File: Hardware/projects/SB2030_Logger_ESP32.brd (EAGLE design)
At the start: 32.7 x 59.7 mm, 20 parts, among them SW1 CKTACTSWITCH, U1 ESP-WROOM-32, U2 MCP2562, U3 NCP1117ST50T3G, U4 NCP1117ST33T3G

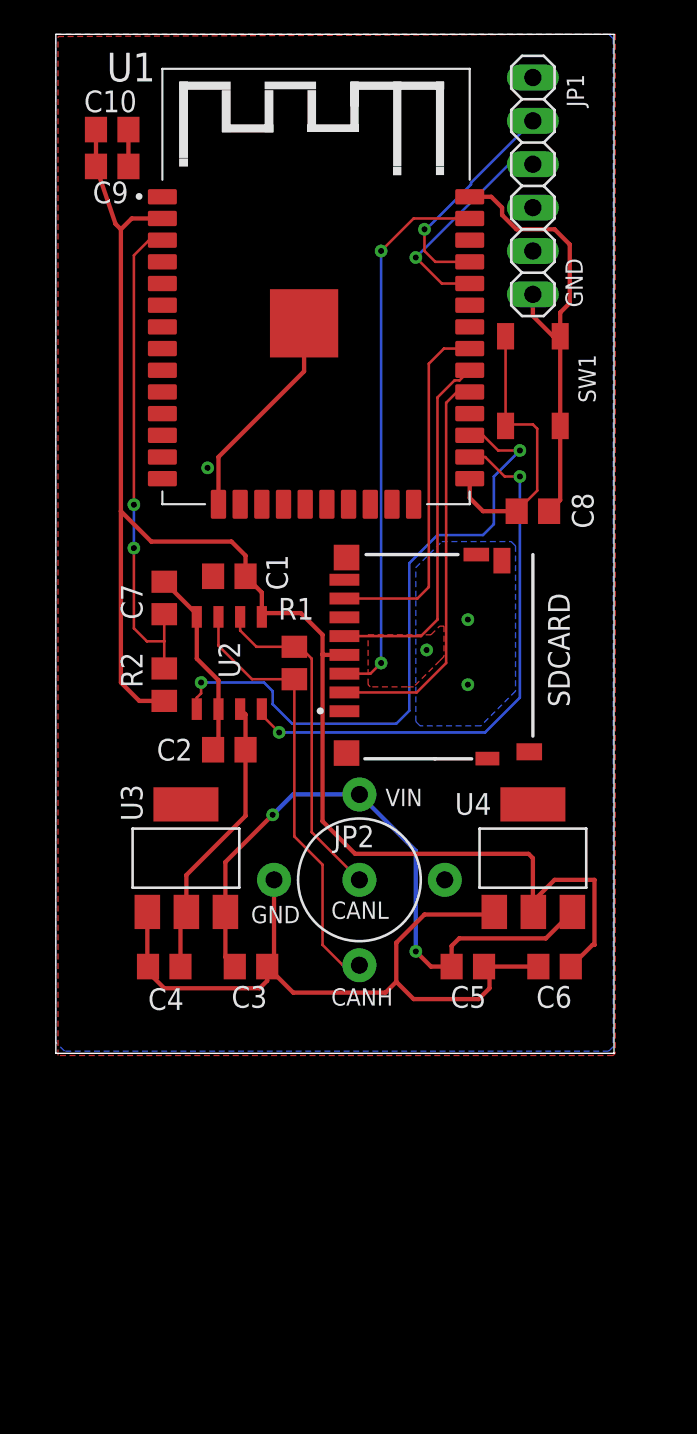
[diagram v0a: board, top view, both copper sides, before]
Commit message: Updates to hardware prototype design to support RS422 input, and added separate RS422 for Arduino Due for testing purposes.
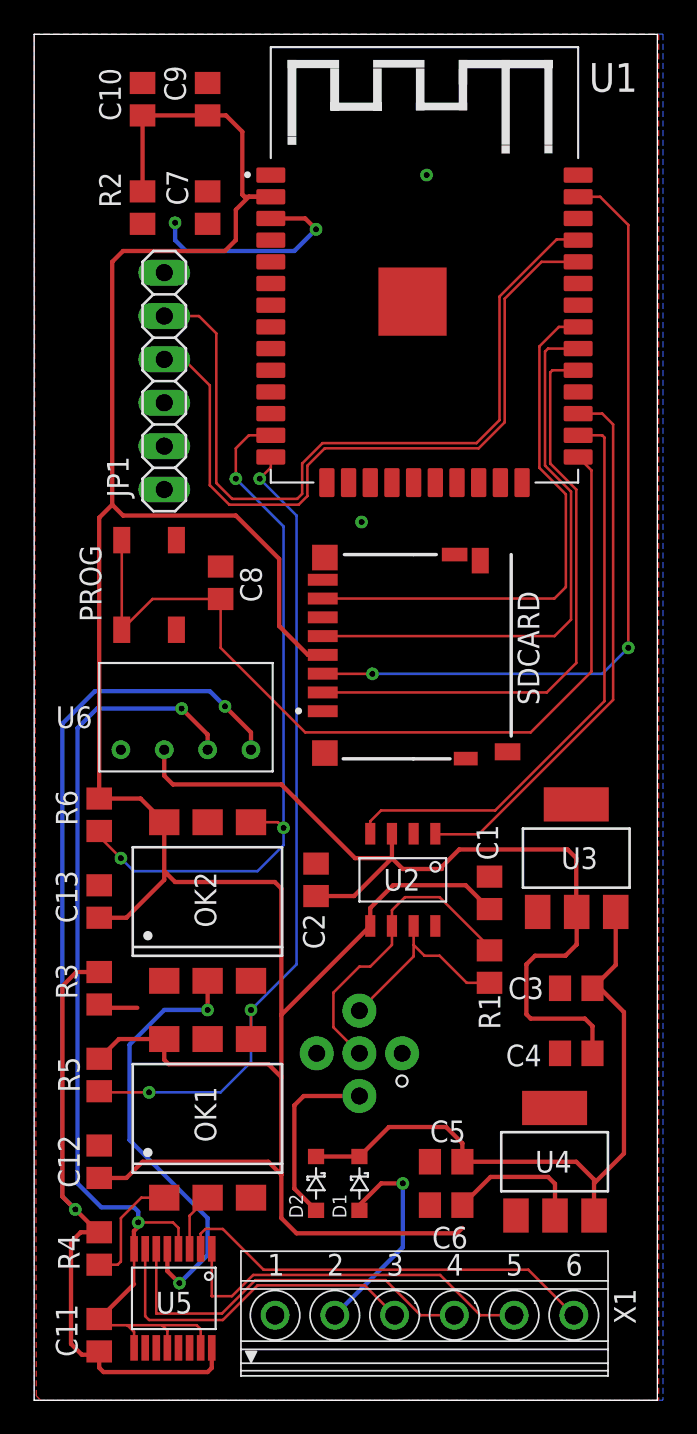
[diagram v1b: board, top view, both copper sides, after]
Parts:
- added C11, C12, C13: 0.1u, rcl:C0805
- added D1, D2: 1N5819, sb2030_logger:SOD123
- added OK1, OK2: H11L1MS, optocoupler:DIL6-SMD
- added R3, R4: 1k2, rcl:R0805
- added R5, R6: 10k, rcl:R0805
- added U5: SN65C1168PWR, sb2030_logger:16-TSSOP
- added U6: (no value), sb2030_logger:RFM-0505S
- added X1: 1751280, con-phoenix-350:1751280
- moved R2 28.0 mm to (6.35, 69.8), turned to 90 degrees
- moved SW1 25.5 mm to (6.73, 47.8)
- moved C4 24.7 mm to (31.8, 20.3)
- moved JP1 24.4 mm to (7.62, 59.7)
- moved C1 24.0 mm to (26.7, 29.7), turned to 90 degrees
- moved C7 23.0 mm to (10.2, 69.8)
- moved U3 22.9 mm to (31.8, 31.8)
- moved R1 21.1 mm to (26.7, 25.4)
- moved C3 19.1 mm to (31.8, 24.1), turned to 180 degrees
- moved C8 18.8 mm to (10.9, 47.9), turned to 90 degrees
- moved U4 17.8 mm to (30.5, 14.0)
- moved U2 16.3 mm to (21.6, 30.5), turned to 180 degrees
- moved C6 15.3 mm to (24.1, 11.4)
- moved C5 11.5 mm to (24.1, 14.0), turned to 180 degrees
- moved JP2 10.2 mm to (19.1, 20.3)
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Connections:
- removed net N$11: C1.2
- new net +12V: D1.1, X1.2
- new net GNDI: C11.2, U5.12, U5.15, U5.4, U5.8, U5.9, U6.3
- new net N$13: OK1.2, U5.3
- new net N$14: OK2.2, U5.5
- new net N$15: OK1.1, R4.1
- new net N$16: OK2.1, R3.1
- new net N$17: U5.2, X1.6
- new net N$18: U5.1, X1.5
- new net N$19: U5.6, X1.4
- new net N$20: U5.7, X1.3
- new net N$21: C11.1, R3.2, R4.2, U5.16, U6.4
- new net N$22: D2.1, JP2.2
- new net RX1: OK1.4, R5.1, U1.14
- new net RX2: OK2.4, R6.1, U1.13
- net +3V3: now also C12.1, C13.1, OK1.6, OK2.6, R5.2, R6.2
- net +5V: now also U6.2
- net GND: now also C1.2, C12.2, C13.2, OK1.5, OK2.5, U6.1, X1.1
- net VIN: now also D1.2, D2.2; no longer JP2.2
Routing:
- net GND: track 98.0 -> 0.00 mm, vias 4 -> 2
- net +3V3: track 93.4 -> 177.0 mm
- net N$21: track 0.00 -> 79.2 mm, vias 0 -> 2
- net GNDI: track 0.00 -> 62.1 mm, vias 0 -> 2
- net RX1: track 0.00 -> 49.1 mm, vias 0 -> 3
- net RX2: track 0.00 -> 41.4 mm, vias 0 -> 3
- net N$12: track 16.8 -> 52.8 mm
- net +5V: track 16.8 -> 52.6 mm
- net RXDATA: track 13.2 -> 45.4 mm, vias 1 -> 0
- net TXDATA: track 12.9 -> 42.4 mm, vias 1 -> 0
- net N$14: track 0.00 -> 26.0 mm, vias 0 -> 2
- net N$17: track 0.00 -> 25.0 mm
- net N$19: track 0.00 -> 22.9 mm
- net N$18: track 0.00 -> 22.0 mm
- net N$20: track 0.00 -> 20.2 mm
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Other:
- board size 32.7 x 59.7 mm -> 36.5 x 80 mm
- board text added: "PROG"
- board text removed: "CANH"
- board text removed: "CANL"
- board text removed: "GND"
- board text removed: "JP2"
- board text removed: "SW1"
- board text removed: "VIN"

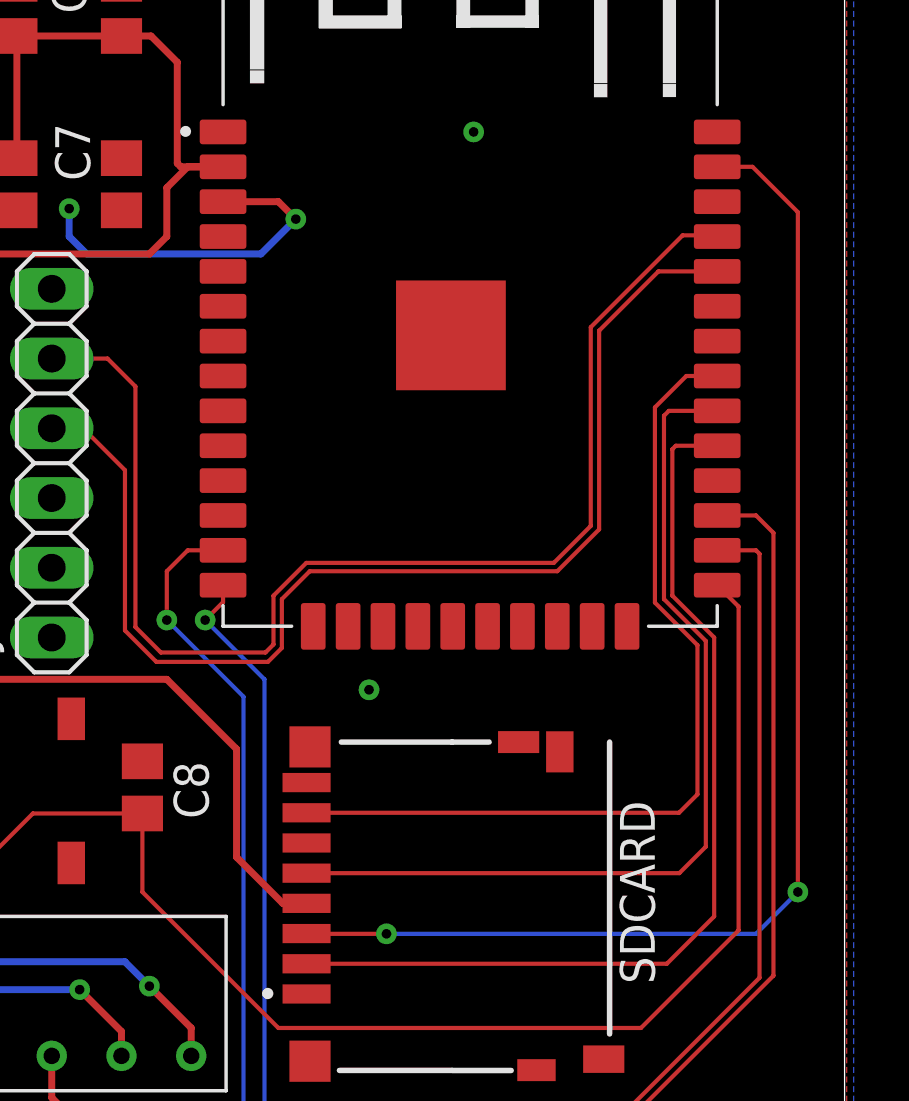
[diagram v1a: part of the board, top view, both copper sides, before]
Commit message: Update to ESP32-based hardware to accommodate NMEA0183 input pins that don't cause boot problems (GPIO12 is used to set Flash voltage on boot, so having an active data stream attached causes all sorts of problems at boot time).
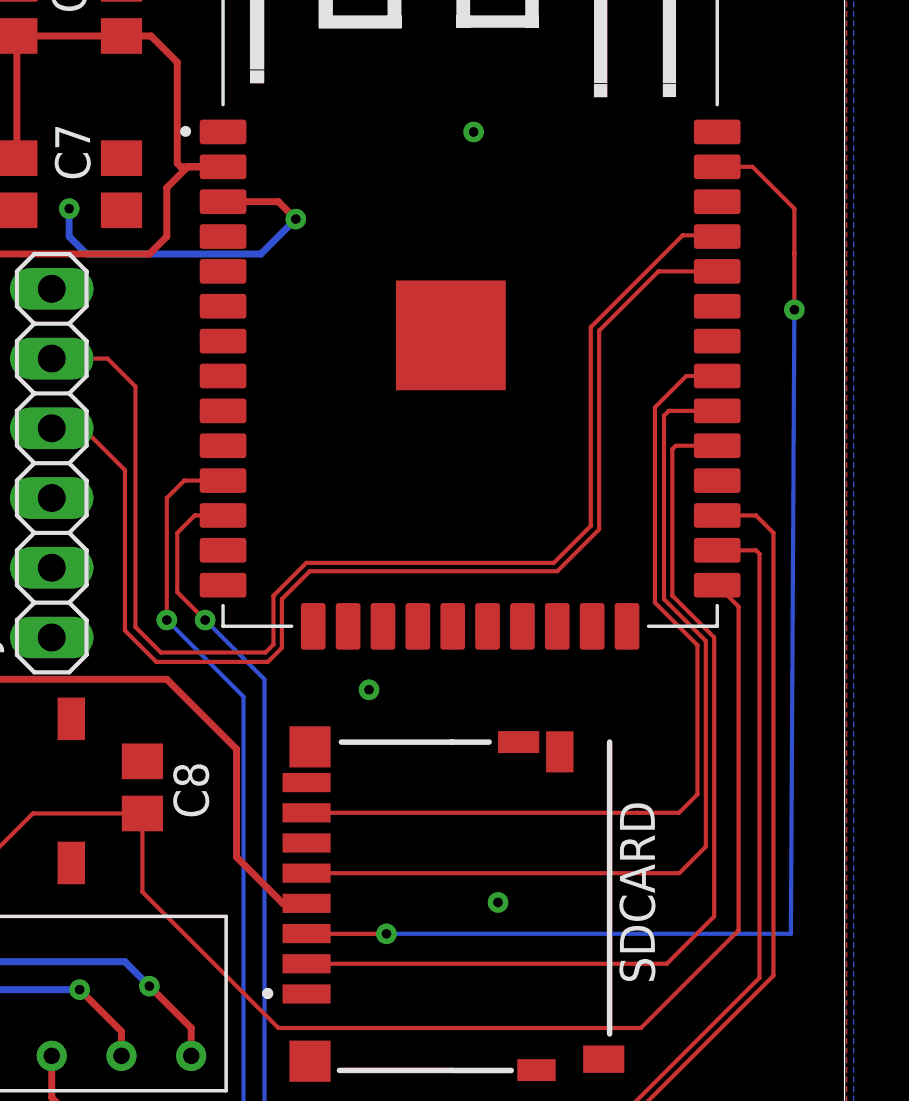
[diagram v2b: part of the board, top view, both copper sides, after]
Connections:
- net RX1: now also U1.12; no longer U1.14
- net RX2: now also U1.11; no longer U1.13
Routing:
- net RX1: track 49.1 -> 53.0 mm
- net RX2: track 41.4 -> 44.0 mm
- net N$8: track 46.9 -> 47.5 mm
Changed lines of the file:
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@@
 <drawing>
 <settings>
-<setting alwaysvectorfont="yes"/>
+<setting alwaysvectorfont="no"/>
 <setting verticaltext="up"/>
 </settings>
@@
 <via x="19.177" y="51.435" extent="1-16" drill="0.35"/>
 <via x="22.987" y="71.755" extent="1-16" drill="0.35"/>
+<via x="23.876" y="43.688" extent="1-16" drill="0.35"/>
 </signal>
 <signal name="+3V3">
@@
 <contactref element="U1" pad="37"/>
 <contactref element="SDCARD" pad="3"/>
-<wire x1="31.86" y1="70.485" x2="33.147" y2="70.485" width="0.1524" layer="1"/>
-<wire x1="33.147" y1="70.485" x2="34.798" y2="68.834" width="0.1524" layer="1"/>
-<wire x1="34.798" y1="68.834" x2="34.798" y2="44.069" width="0.1524" layer="1"/>
-<via x="34.798" y="44.069" extent="1-16" drill="0.35"/>
-<wire x1="34.798" y1="44.069" x2="33.274" y2="42.545" width="0.1524" layer="16"/>
-<wire x1="33.274" y1="42.545" x2="19.812" y2="42.545" width="0.1524" layer="16"/>
+<wire x1="33.147" y1="70.485" x2="31.86" y2="70.485" width="0.1524" layer="1"/>
+<wire x1="34.671" y1="67.35618125" x2="34.671" y2="67.31" width="0.1524" layer="1"/>
+<via x="34.671" y="65.278" extent="1-16" drill="0.35"/>
+<wire x1="34.671" y1="67.31" x2="34.671" y2="65.278" width="0.1524" layer="1"/>
+<wire x1="34.671" y1="65.278" x2="34.544" y2="42.545" width="0.1524" layer="16"/>
+<wire x1="34.544" y1="42.545" x2="19.812" y2="42.545" width="0.1524" layer="16"/>
 <via x="19.812" y="42.545" extent="1-16" drill="0.35"/>
 <wire x1="19.812" y1="42.545" x2="16.912" y2="42.545" width="0.1524" layer="1"/>
 <wire x1="16.912" y1="42.545" x2="16.902" y2="42.555" width="0.1524" layer="1"/>
+<wire x1="34.671" y1="67.35618125" x2="34.671" y2="68.961" width="0.1524" layer="1"/>
+<wire x1="34.671" y1="68.961" x2="33.147" y2="70.485" width="0.1524" layer="1"/>
 </signal>
 <signal name="N$9">
@@
 </signal>
 <signal name="RX1">
-<contactref element="U1" pad="14"/>
 <contactref element="OK1" pad="4"/>
 <contactref element="R5" pad="1"/>
@@
 <wire x1="15.367" y1="51.816" x2="13.208" y2="53.975" width="0.1524" layer="16"/>
 <via x="13.208" y="53.975" extent="1-16" drill="0.35"/>
-<wire x1="13.208" y1="53.975" x2="13.86" y2="54.627" width="0.1524" layer="1"/>
-<wire x1="13.86" y1="54.627" x2="13.86" y2="55.245" width="0.1524" layer="1"/>
+<contactref element="U1" pad="12"/>
+<wire x1="13.208" y1="53.975" x2="12.192" y2="54.991" width="0.1524" layer="1"/>
+<wire x1="12.192" y1="54.991" x2="12.192" y2="57.15" width="0.1524" layer="1"/>
+<wire x1="12.192" y1="57.15" x2="12.827" y2="57.785" width="0.1524" layer="1"/>
+<wire x1="12.827" y1="57.785" x2="13.86" y2="57.785" width="0.1524" layer="1"/>
 </signal>
 <signal name="RX2">
-<contactref element="U1" pad="13"/>
 <contactref element="OK2" pad="4"/>
 <contactref element="R6" pad="1"/>
@@
 <wire x1="14.605" y1="51.181" x2="11.811" y2="53.975" width="0.1524" layer="16"/>
 <via x="11.811" y="53.975" extent="1-16" drill="0.35"/>
-<wire x1="11.811" y1="53.975" x2="11.811" y2="55.753" width="0.1524" layer="1"/>
-<wire x1="11.811" y1="55.753" x2="12.573" y2="56.515" width="0.1524" layer="1"/>
-<wire x1="12.573" y1="56.515" x2="13.86" y2="56.515" width="0.1524" layer="1"/>
+<contactref element="U1" pad="11"/>
+<wire x1="12.446" y1="59.055" x2="13.86" y2="59.055" width="0.1524" layer="1"/>
+<wire x1="11.811" y1="53.975" x2="11.811" y2="58.42" width="0.1524" layer="1"/>
+<wire x1="11.811" y1="58.42" x2="12.446" y2="59.055" width="0.1524" layer="1"/>
 </signal>
 <signal name="N$22">

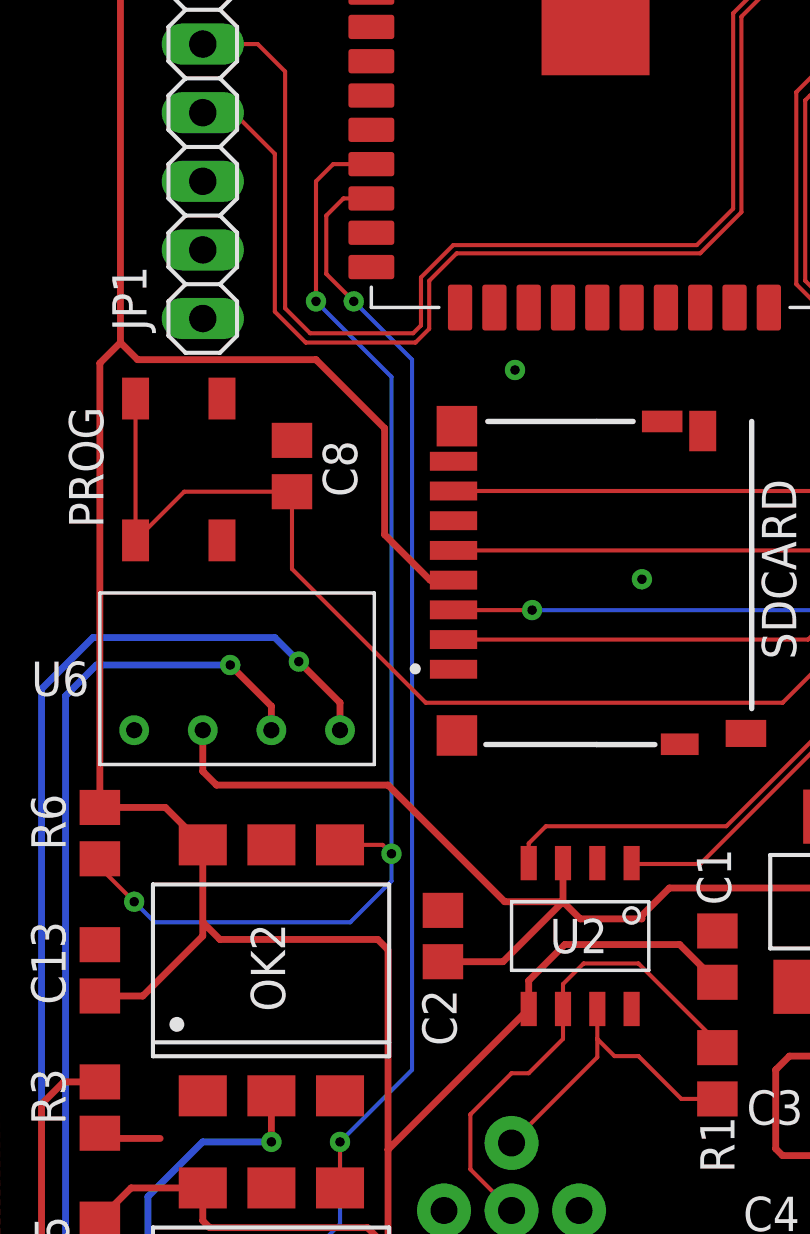
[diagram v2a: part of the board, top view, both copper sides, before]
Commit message: Updated schematic for ESP32, and source code, to reflect new choice of UART receiver pins.
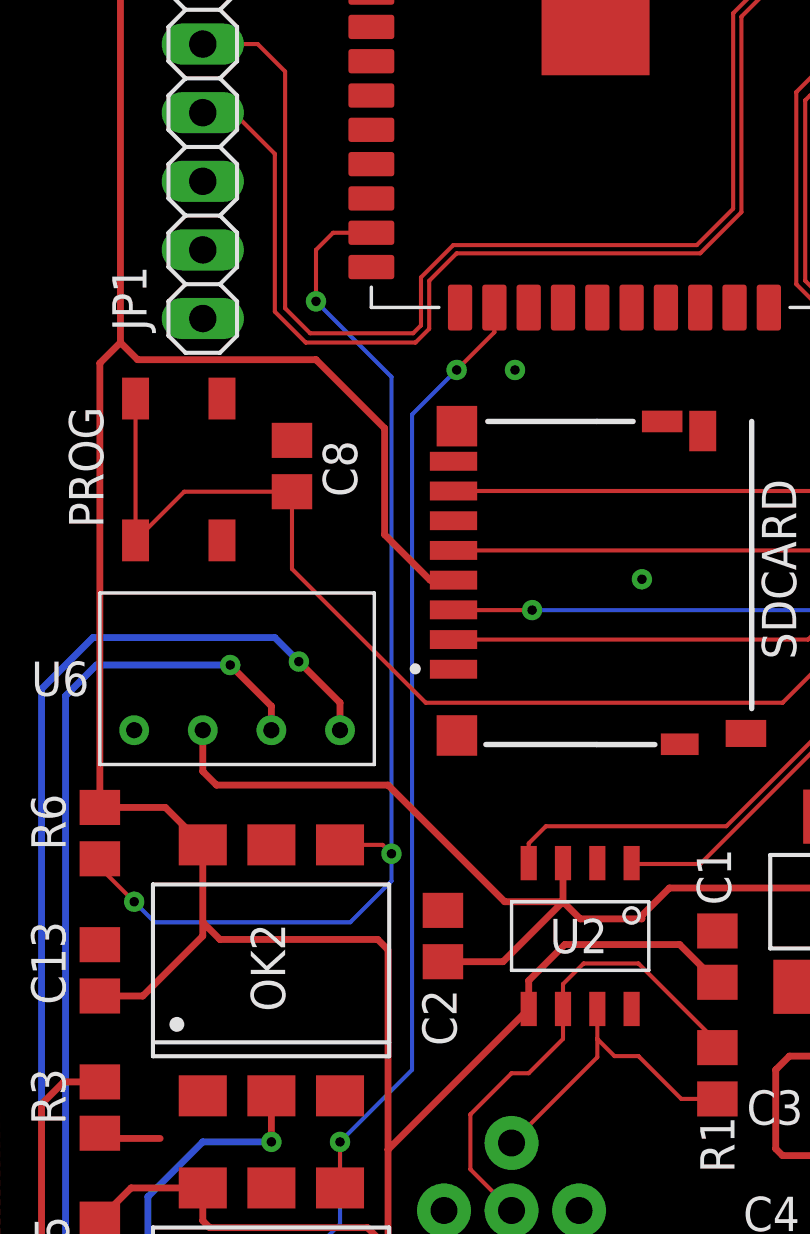
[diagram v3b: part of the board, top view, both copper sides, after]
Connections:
- net RX1: now also U1.16; no longer U1.12
- net RX2: now also U1.13; no longer U1.11
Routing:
- net RX1: track 53.0 -> 47.7 mm
- net RX2: track 44.0 -> 41.5 mm
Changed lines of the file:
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@@
 <wire x1="3.876" y1="18.034" x2="3.81" y2="18.1" width="0.1524" layer="1"/>
 <wire x1="12.7" y1="22.86" x2="15.367" y2="25.527" width="0.1524" layer="16"/>
-<wire x1="15.367" y1="25.527" x2="15.367" y2="51.816" width="0.1524" layer="16"/>
-<wire x1="15.367" y1="51.816" x2="13.208" y2="53.975" width="0.1524" layer="16"/>
-<via x="13.208" y="53.975" extent="1-16" drill="0.35"/>
-<contactref element="U1" pad="12"/>
-<wire x1="13.208" y1="53.975" x2="12.192" y2="54.991" width="0.1524" layer="1"/>
-<wire x1="12.192" y1="54.991" x2="12.192" y2="57.15" width="0.1524" layer="1"/>
-<wire x1="12.192" y1="57.15" x2="12.827" y2="57.785" width="0.1524" layer="1"/>
-<wire x1="12.827" y1="57.785" x2="13.86" y2="57.785" width="0.1524" layer="1"/>
+<wire x1="15.367" y1="25.527" x2="15.367" y2="49.784" width="0.1524" layer="16"/>
+<wire x1="15.367" y1="49.784" x2="17.018" y2="51.435" width="0.1524" layer="16"/>
+<via x="17.018" y="51.435" extent="1-16" drill="0.35"/>
+<contactref element="U1" pad="16"/>
+<wire x1="17.018" y1="51.435" x2="18.415" y2="52.832" width="0.1524" layer="1"/>
+<wire x1="18.415" y1="52.832" x2="18.415" y2="53.745" width="0.1524" layer="1"/>
 </signal>
 <signal name="RX2">
@@
 <wire x1="14.605" y1="51.181" x2="11.811" y2="53.975" width="0.1524" layer="16"/>
 <via x="11.811" y="53.975" extent="1-16" drill="0.35"/>
-<contactref element="U1" pad="11"/>
-<wire x1="12.446" y1="59.055" x2="13.86" y2="59.055" width="0.1524" layer="1"/>
-<wire x1="11.811" y1="53.975" x2="11.811" y2="58.42" width="0.1524" layer="1"/>
-<wire x1="11.811" y1="58.42" x2="12.446" y2="59.055" width="0.1524" layer="1"/>
+<wire x1="11.811" y1="53.975" x2="11.811" y2="55.88" width="0.1524" layer="1"/>
+<contactref element="U1" pad="13"/>
+<wire x1="12.446" y1="56.515" x2="13.86" y2="56.515" width="0.1524" layer="1"/>
+<wire x1="11.811" y1="55.88" x2="12.446" y2="56.515" width="0.1524" layer="1"/>
 </signal>
 <signal name="N$22">
